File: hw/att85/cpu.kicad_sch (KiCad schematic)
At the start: 6 parts, among them J1 Conn_01x06, U1 STM32G030K8Tx, U2 74AHCT125

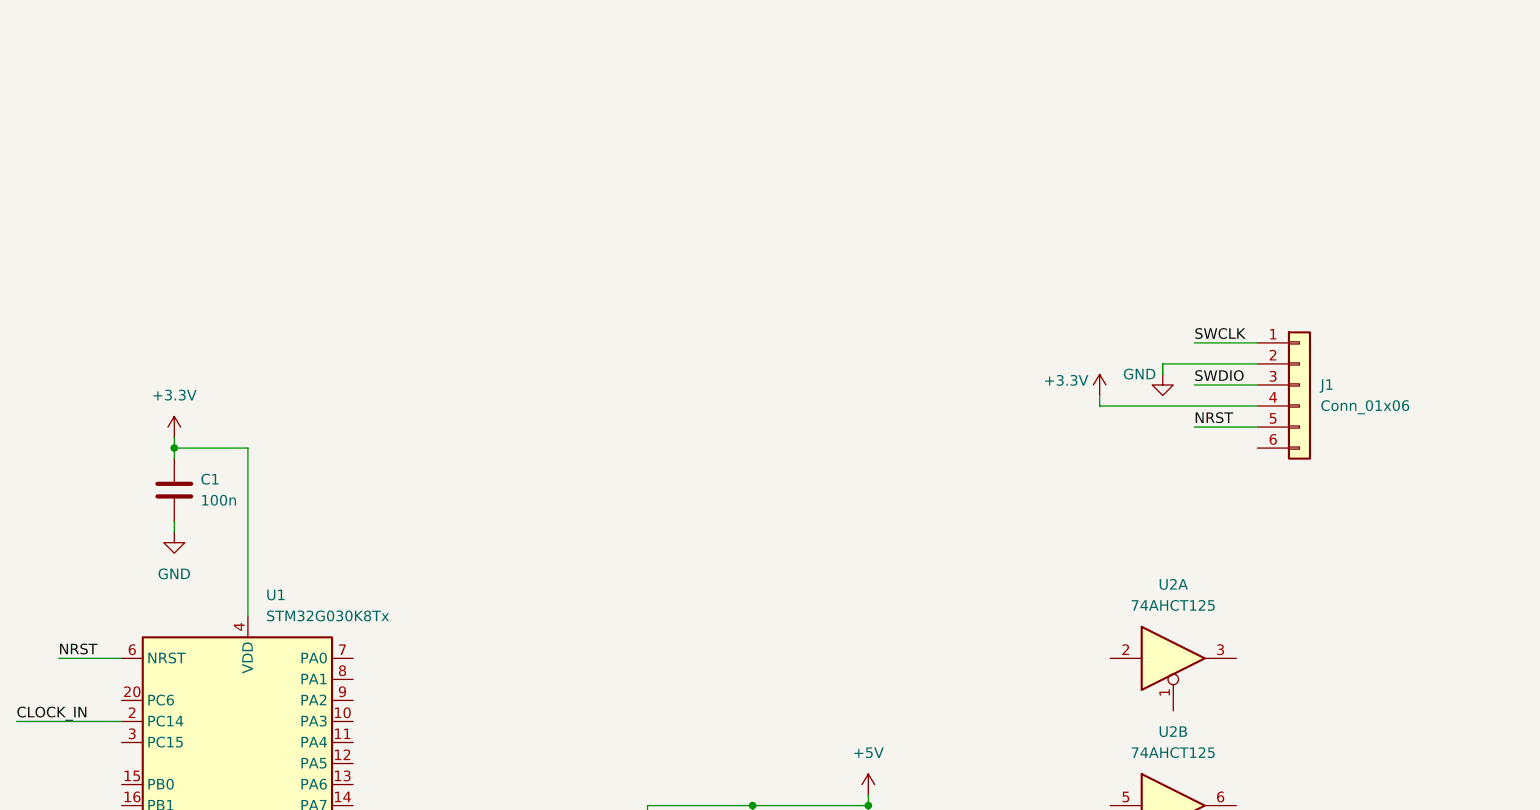
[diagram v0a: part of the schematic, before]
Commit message: chore(hw): update debug port pinout
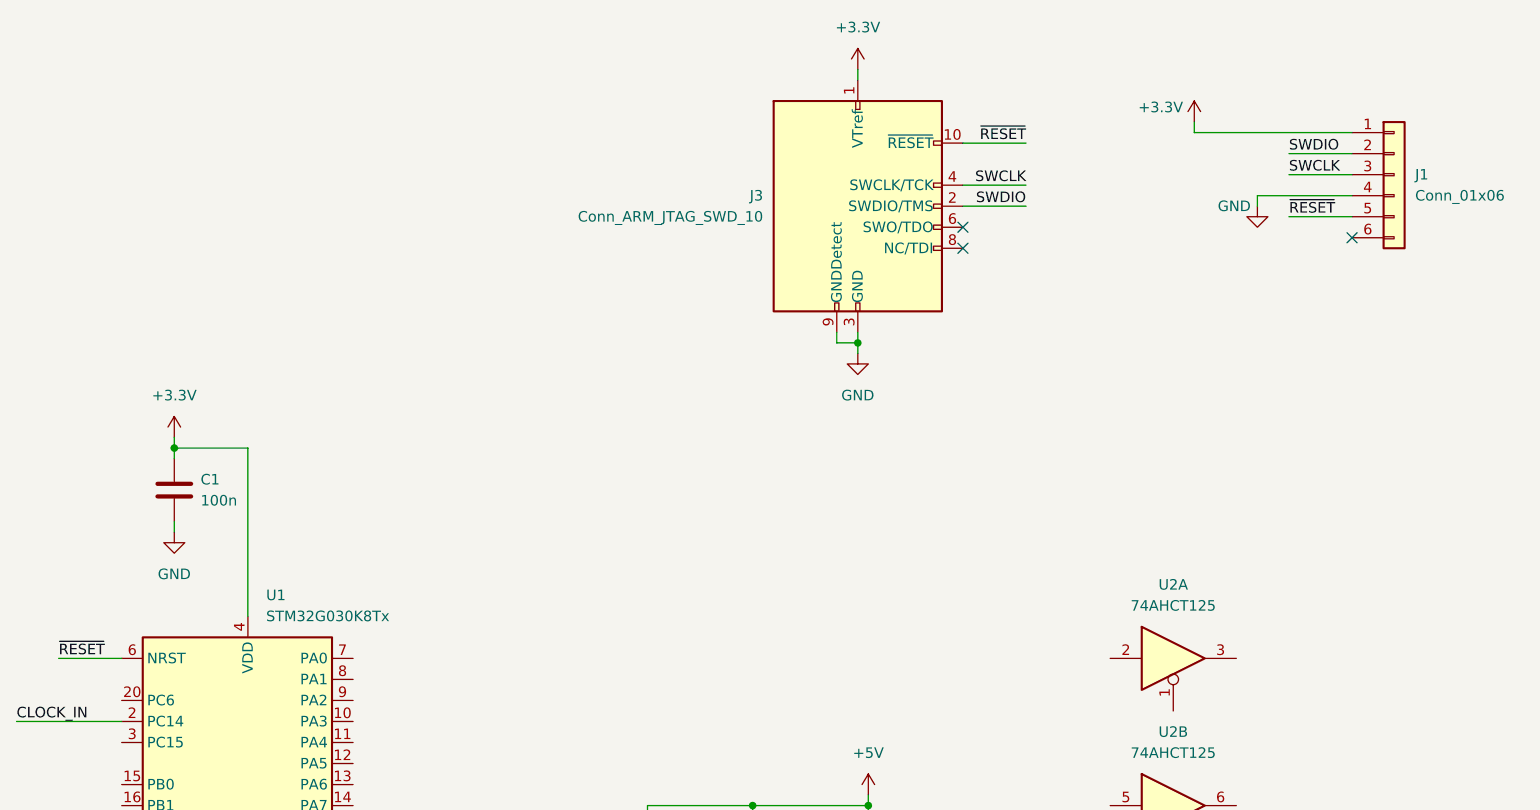
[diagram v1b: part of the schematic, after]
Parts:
- added J3: Conn_ARM_JTAG_SWD_10, Connector:Tag-Connect_TC2050-IDC-FP_2x05_P1.27mm_Vertical, symbol Connector:Conn_ARM_JTAG_SWD_10
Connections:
- net +3.3V: now also J1.1 (Pin_1), J3.1 (VTref); no longer J1.4 (Pin_4)
- net GND: now also J1.4 (Pin_4), J3.3 (GND), J3.5 (GND), J3.9 (GNDDetect); no longer J1.2 (Pin_2)
- net SWCLK: now also J1.3 (Pin_3), J3.4 (SWCLK/TCK); no longer J1.1 (Pin_1)
- net SWDIO: now also J1.2 (Pin_2), J3.2 (SWDIO/TMS); no longer J1.3 (Pin_3)
- net NRST renamed ~{RESET}
- net ~{RESET}: now also J3.10 (~{RESET})
- no-connect marks 0 -> 3
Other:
- moved on the sheet: J1

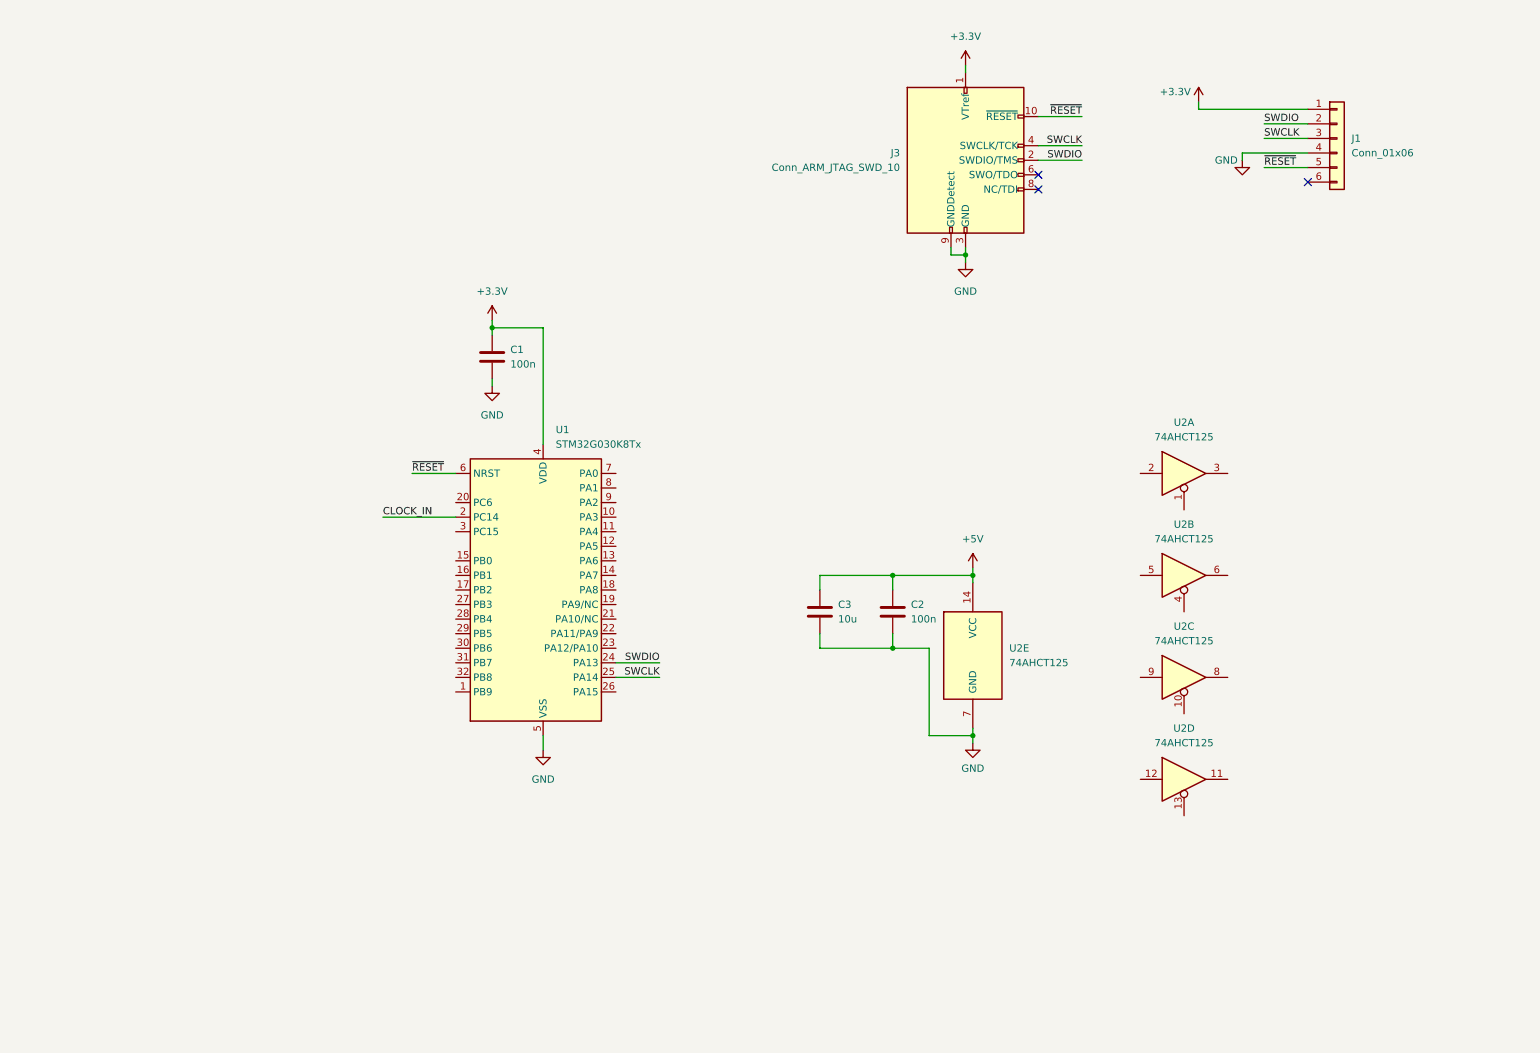
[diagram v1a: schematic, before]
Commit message: chore(hw): organize schematics into sheets, sync with layout
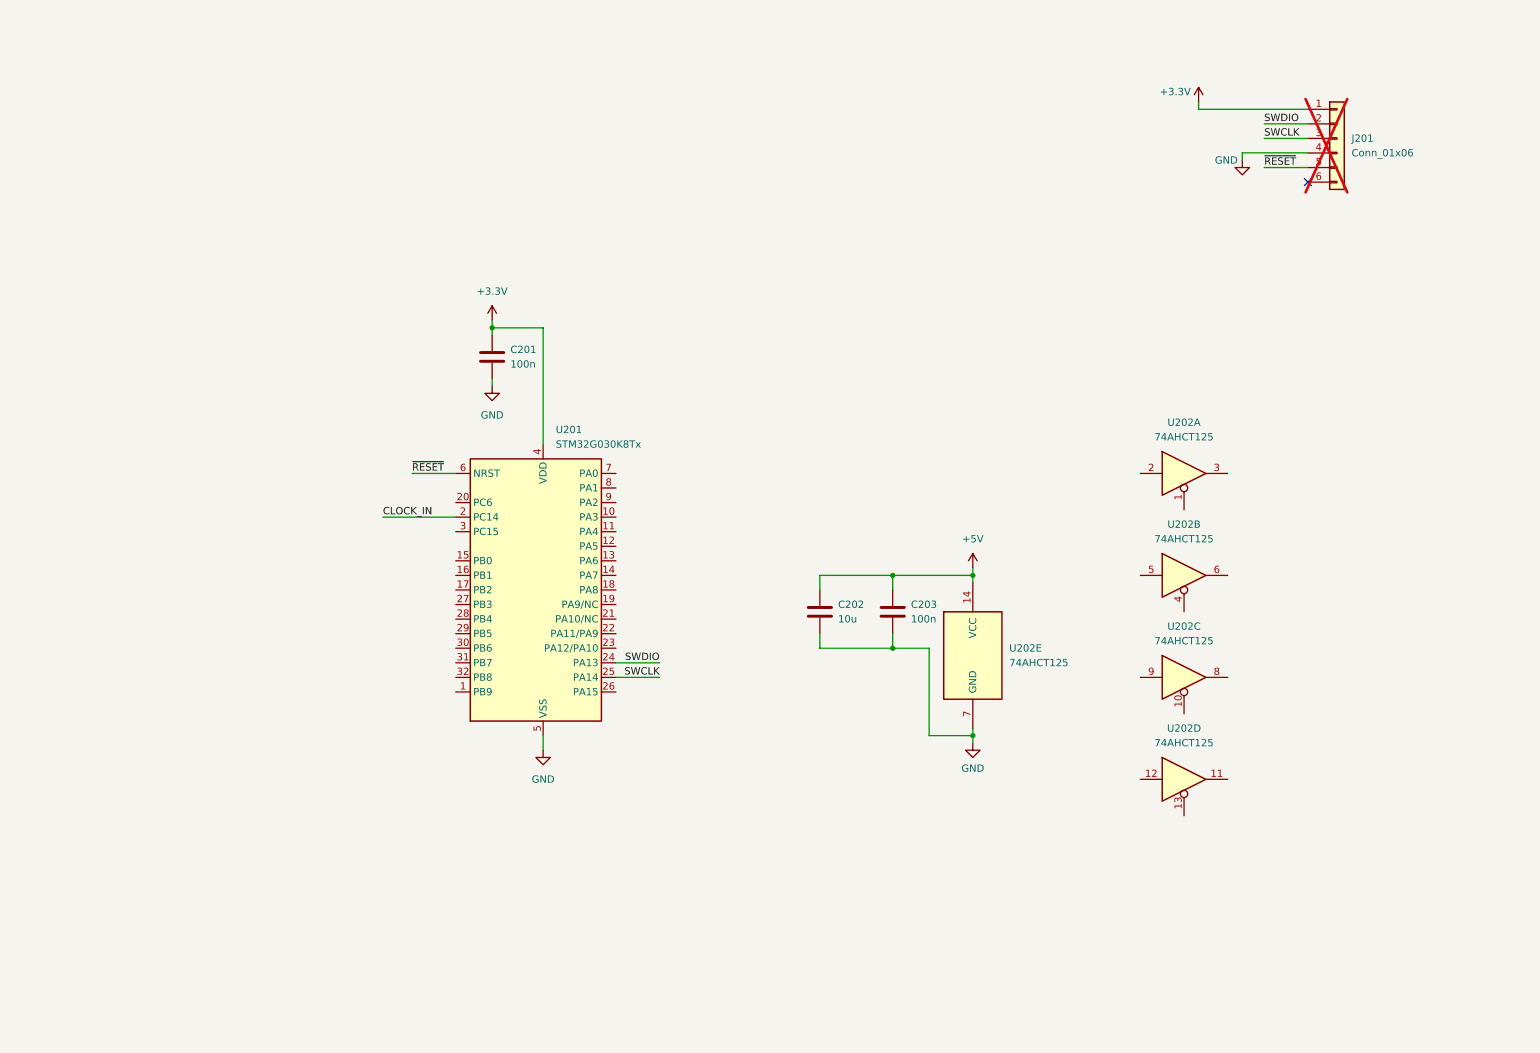
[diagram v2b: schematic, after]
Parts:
- removed J3: Conn_ARM_JTAG_SWD_10, Connector:Tag-Connect_TC2050-IDC-FP_2x05_P1.27mm_Vertical, symbol Connector:Conn_ARM_JTAG_SWD_10
- J201: renamed from J1; footprint (none) -> Connector_PinSocket_2.54mm:PinSocket_1x06_P2.54mm_Vertical; now not fitted
- U202: renamed from U2; footprint (none) -> Package_SO:SOIC-14_3.9x8.7mm_P1.27mm
- renumbered C1 to C201, C3 to C202, C2 to C203, U1 to U201
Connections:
- no-connect marks 3 -> 1

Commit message: chore(hw): wired basic connections, organized main sheet
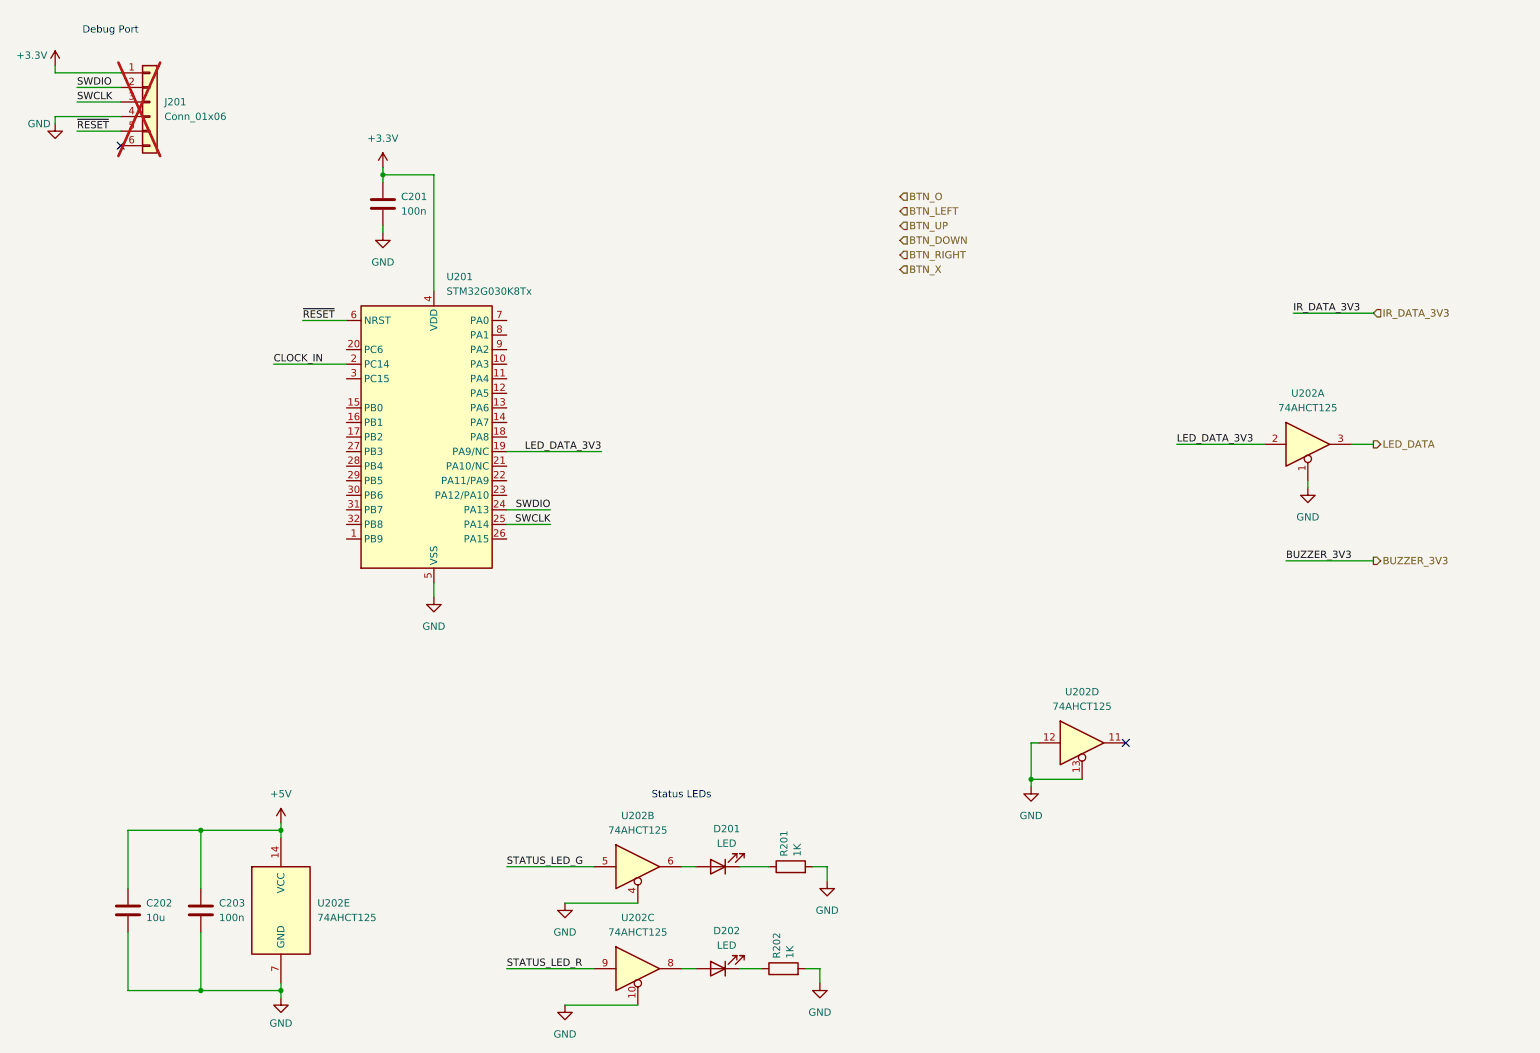
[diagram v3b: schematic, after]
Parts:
- added D201, D202: LED, LED_SMD:LED_0805_2012Metric_Pad1.15x1.40mm_HandSolder, symbol Device:LED
- added R201, R202: 1K, Resistor_SMD:R_0805_2012Metric_Pad1.20x1.40mm_HandSolder, symbol Device:R
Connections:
- net GND: now also U202.1, U202.10, U202.12, U202.13, U202.4, R201.2, R202.2
- net LED_DATA_3V3: now reaches U201.19 (PA9/NC)
- net LED_DATA_3V3: now also U202.2
- net LED_DATA: now reaches U202.3
- net at U202.8: now also D202.2 (A)
- net STATUS_LED_R: now reaches U202.9
- net STATUS_LED_G: now reaches U202.5
- net at U202.6: now also D201.2 (A)
- new net: D202.1 (K), R202.1
- new net: D201.1 (K), R201.1
- no-connect marks 1 -> 2
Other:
- note added: "Debug Port"
- note added: "Status LEDs"
- moved on the sheet: C201, C202, C203, J201, U201, U202A, U202B, U202C, U202D, U202E

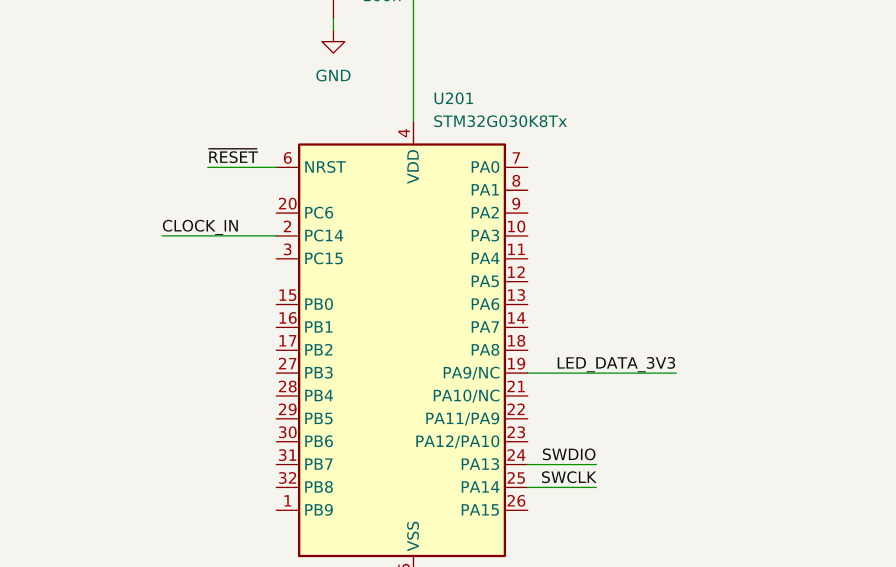
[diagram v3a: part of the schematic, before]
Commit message: chore(hw): connect IR data CPU pin
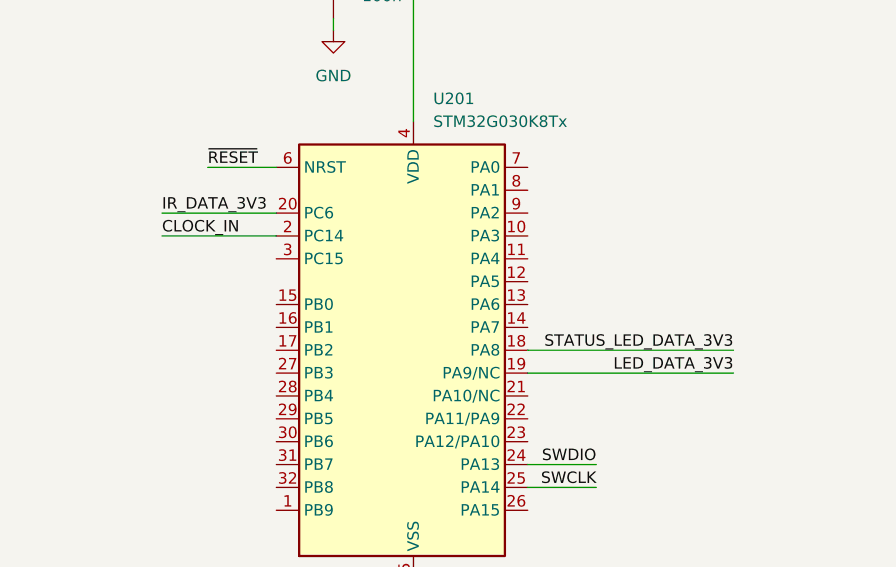
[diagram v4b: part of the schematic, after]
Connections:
- net IR_DATA_3V3: now also U201.20 (PC6)
- net STATUS_LED_DATA_3V3: now reaches U201.18 (PA8)
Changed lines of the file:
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@@
+	(wire
+		(pts
+			(xy 106.68 91.44) (xy 129.54 91.44)
+		)
+		(stroke
+			(width 0)
+			(type default)
+		)
+	)
 	(wire
 		(pts
@@
 	(wire
 		(pts
+			(xy 66.04 76.2) (xy 78.74 76.2)
+		)
+		(stroke
+			(width 0)
+			(type default)
+		)
+	)
+	(wire
+		(pts
 			(xy 39.37 30.48) (xy 31.75 30.48)
 		)
@@
 	(wire
 		(pts
-			(xy 106.68 93.98) (xy 123.19 93.98)
+			(xy 106.68 93.98) (xy 129.54 93.98)
 		)
 		(stroke
@@
 	)
 	(label "LED_DATA_3V3"
-		(at 123.19 93.98 180)
+		(at 129.54 93.98 180)
 		(fields_autoplaced yes)
 		(effects
@@
 			)
 			(justify right bottom)
+		)
+	)
+	(label "IR_DATA_3V3"
+		(at 66.04 76.2 0)
+		(fields_autoplaced yes)
+		(effects
+			(font
+				(size 1.27 1.27)
+			)
+			(justify left bottom)
 		)
 	)
@@
 		)
 	)
+	(label "STATUS_LED_DATA_3V3"
+		(at 129.54 91.44 180)
+		(fields_autoplaced yes)
+		(effects
+			(font
+				(size 1.27 1.27)
+			)
+			(justify right bottom)
+		)
+	)
